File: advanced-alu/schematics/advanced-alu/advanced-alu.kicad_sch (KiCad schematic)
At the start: 3 parts

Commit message: updated documentation
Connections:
- net CMPi renamed CMPs
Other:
- sheet Comparison and Test Unit ports: added CMPs; removed CMPi
- title: (none) -> Advanced Arithmetic Logic Unit
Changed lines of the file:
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@@
 (kicad_sch (version 20211123) (generator eeschema)
   (paper "A4")
+  (title_block
+    (title "Advanced Arithmetic Logic Unit")
+  )
   (junction (at 259.715 77.47) (diameter 0) (color 0 0 0 0)
   )
@@
     (effects (font (size 1.27 1.27)) (justify left))
   )
-  (hierarchical_label "CMPi" (shape input) (at 272.415 77.47 0)
+  (hierarchical_label "CMPs" (shape input) (at 272.415 77.47 0)
     (effects (font (size 1.27 1.27)) (justify left))
   )
@@
       (effects (font (size 1.27 1.27)) (justify right))
     )
-    (pin "CMPi" input (at 122.555 147.32 0)
-      (effects (font (size 1.27 1.27)) (justify right))
-    )
+    (pin "CMPs" input (at 122.555 147.32 0)
+      (effects (font (size 1.27 1.27)) (justify right))
+    )

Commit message: returned temp registr to being 8-bit
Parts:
- gave numbers to parts that had none: 3
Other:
- sheet Arithmetic Logic Unit ports: added TMP_[0..7]; removed LO_TMP_[0..7]
- sheet Comparison and Test Unit ports: added TMP_[0..7]; removed HI_TMP_[0..7]
- sheet Temp Register - 16 bit ports: added TMP_[0..7]; removed HI_TMP_[0..7], HI~{LO}, LO_TMP_[0..7]

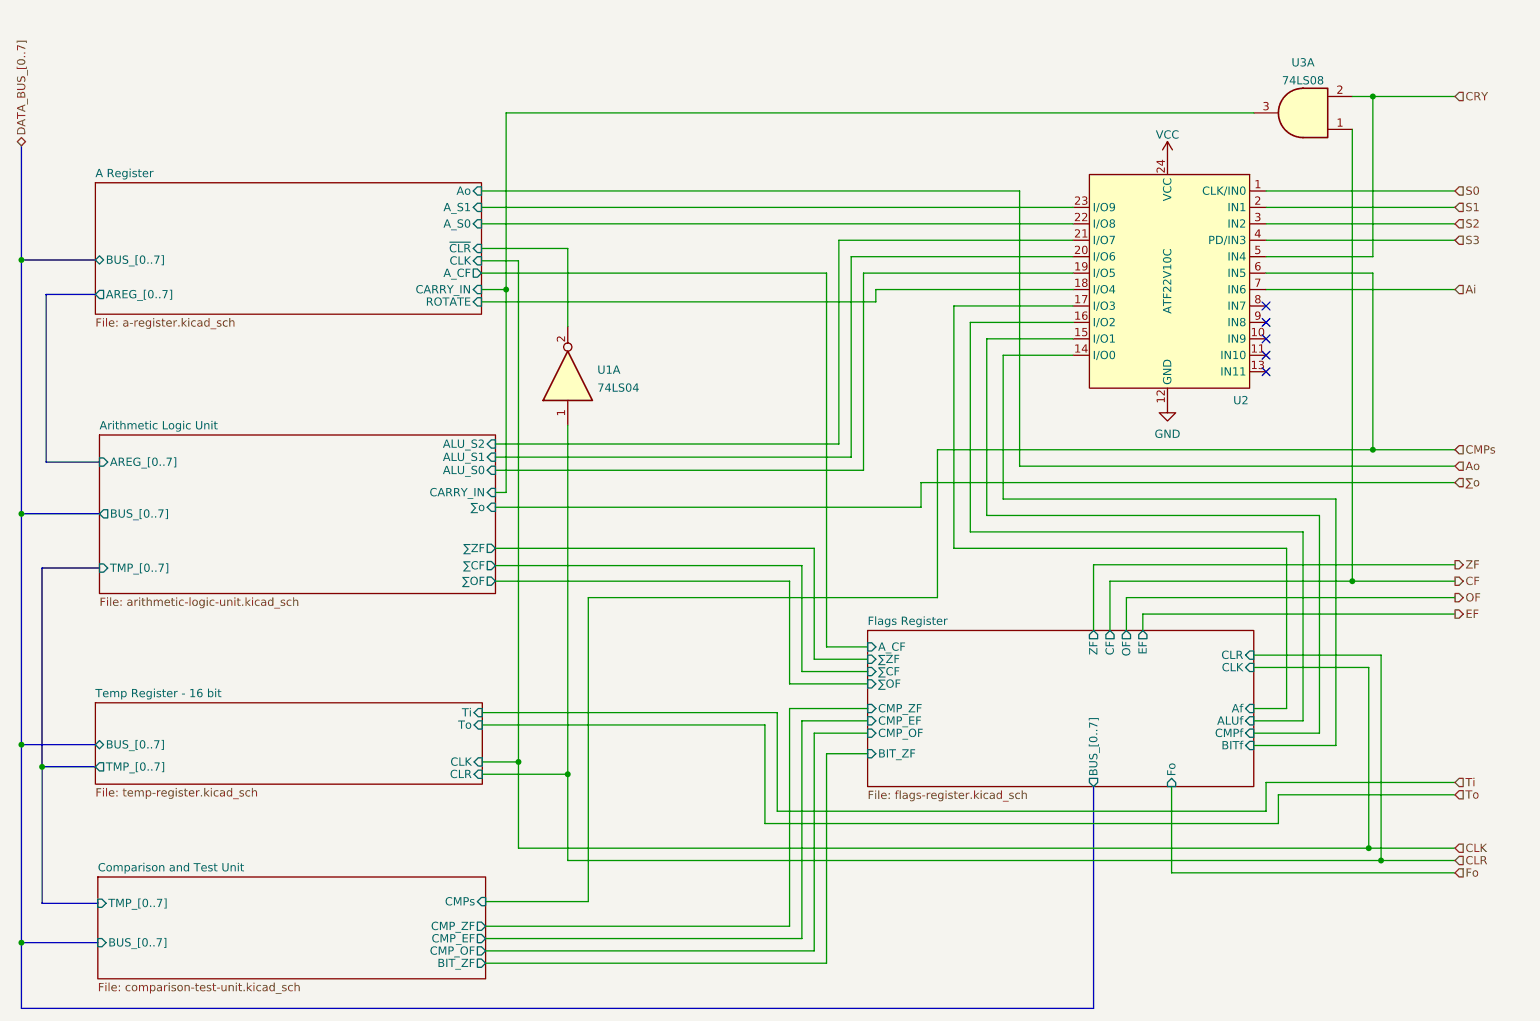
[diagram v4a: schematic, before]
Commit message: updated design to properly handle subtractions
Also added ability to do an arithmetic right shift.
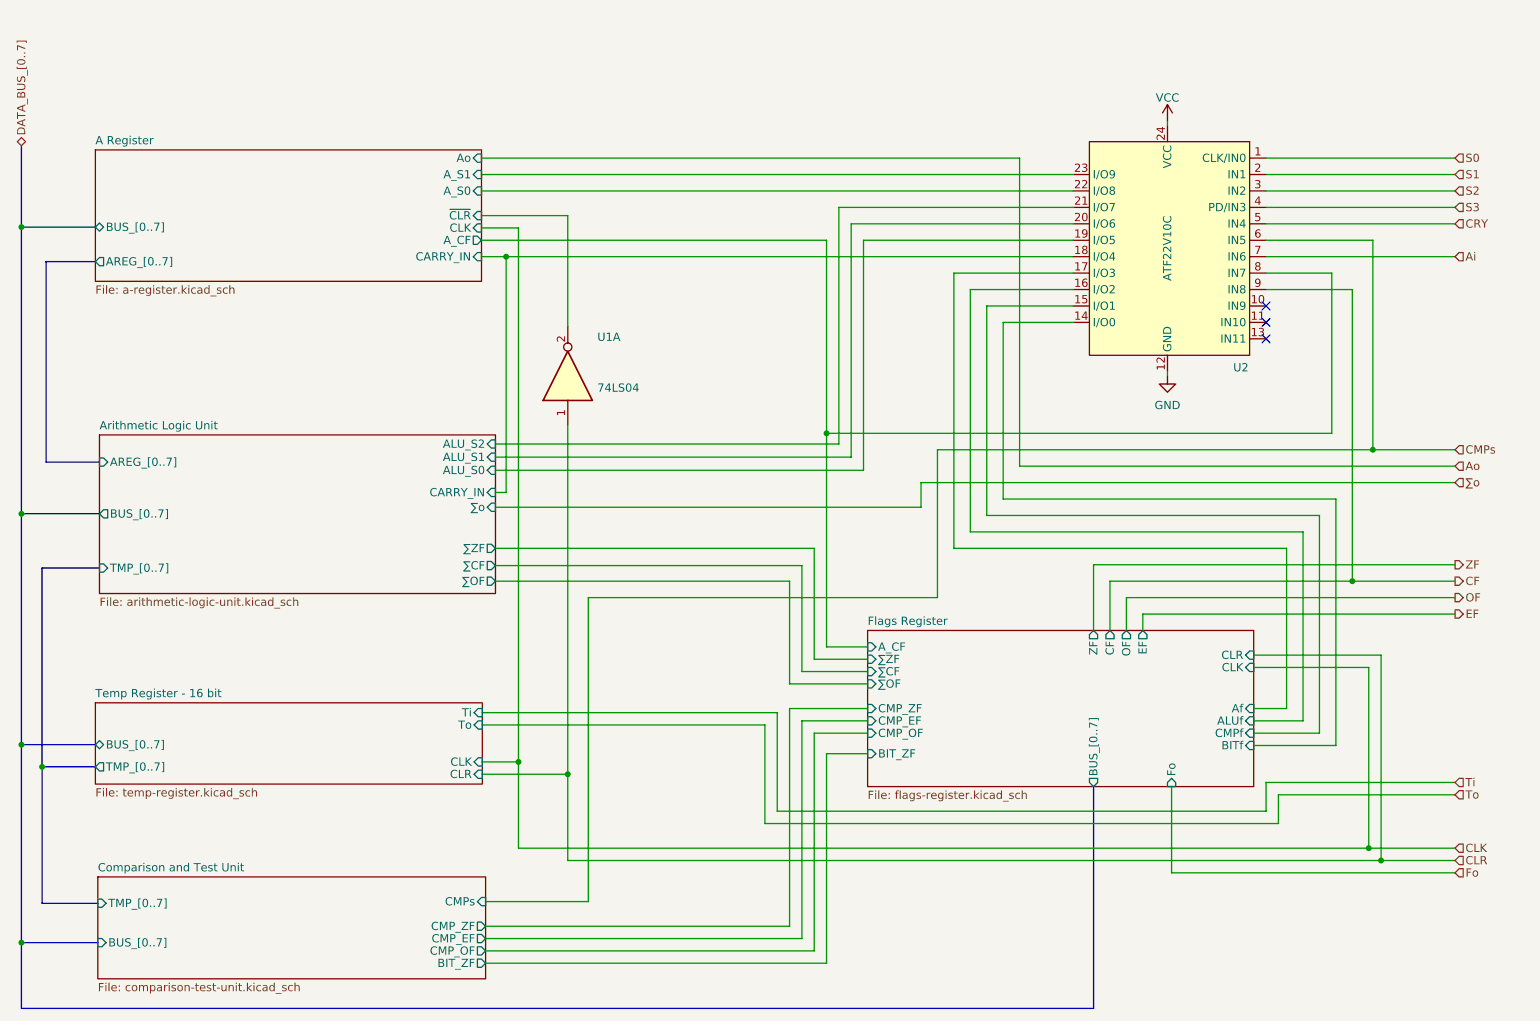
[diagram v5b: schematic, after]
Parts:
- removed U3: 74LS08, symbol 74xx:74LS08
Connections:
- net A Register/ROTATE is gone; now on net A Register/CARRY_IN: U2.18 (I/O4)
- net A Register/A_CF: now also U2.8 (IN7)
- net CF: now also U2.9 (IN8)
- no-connect marks 5 -> 3
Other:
- sheet A Register ports: added none; removed ROTATE
- moved on the sheet: U2
